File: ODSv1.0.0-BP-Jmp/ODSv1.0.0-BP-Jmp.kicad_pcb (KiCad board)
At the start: 2 copper layers, 150 x 150 mm, 53 parts, among them J1 Conn_01x16, J10 Conn_02x10_Odd_Even, J11 Conn_02x10_Odd_Even, J12 Conn_02x10_Odd_Even, J13 Conn_02x10_Odd_Even, J14 Conn_02x10_Odd_Even, J2 Conn_02x60_Odd_Even, J3 Conn_02x60_Odd_Even, J4 Conn_02x10_Odd_Even, J5 Conn_02x10_Odd_Even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

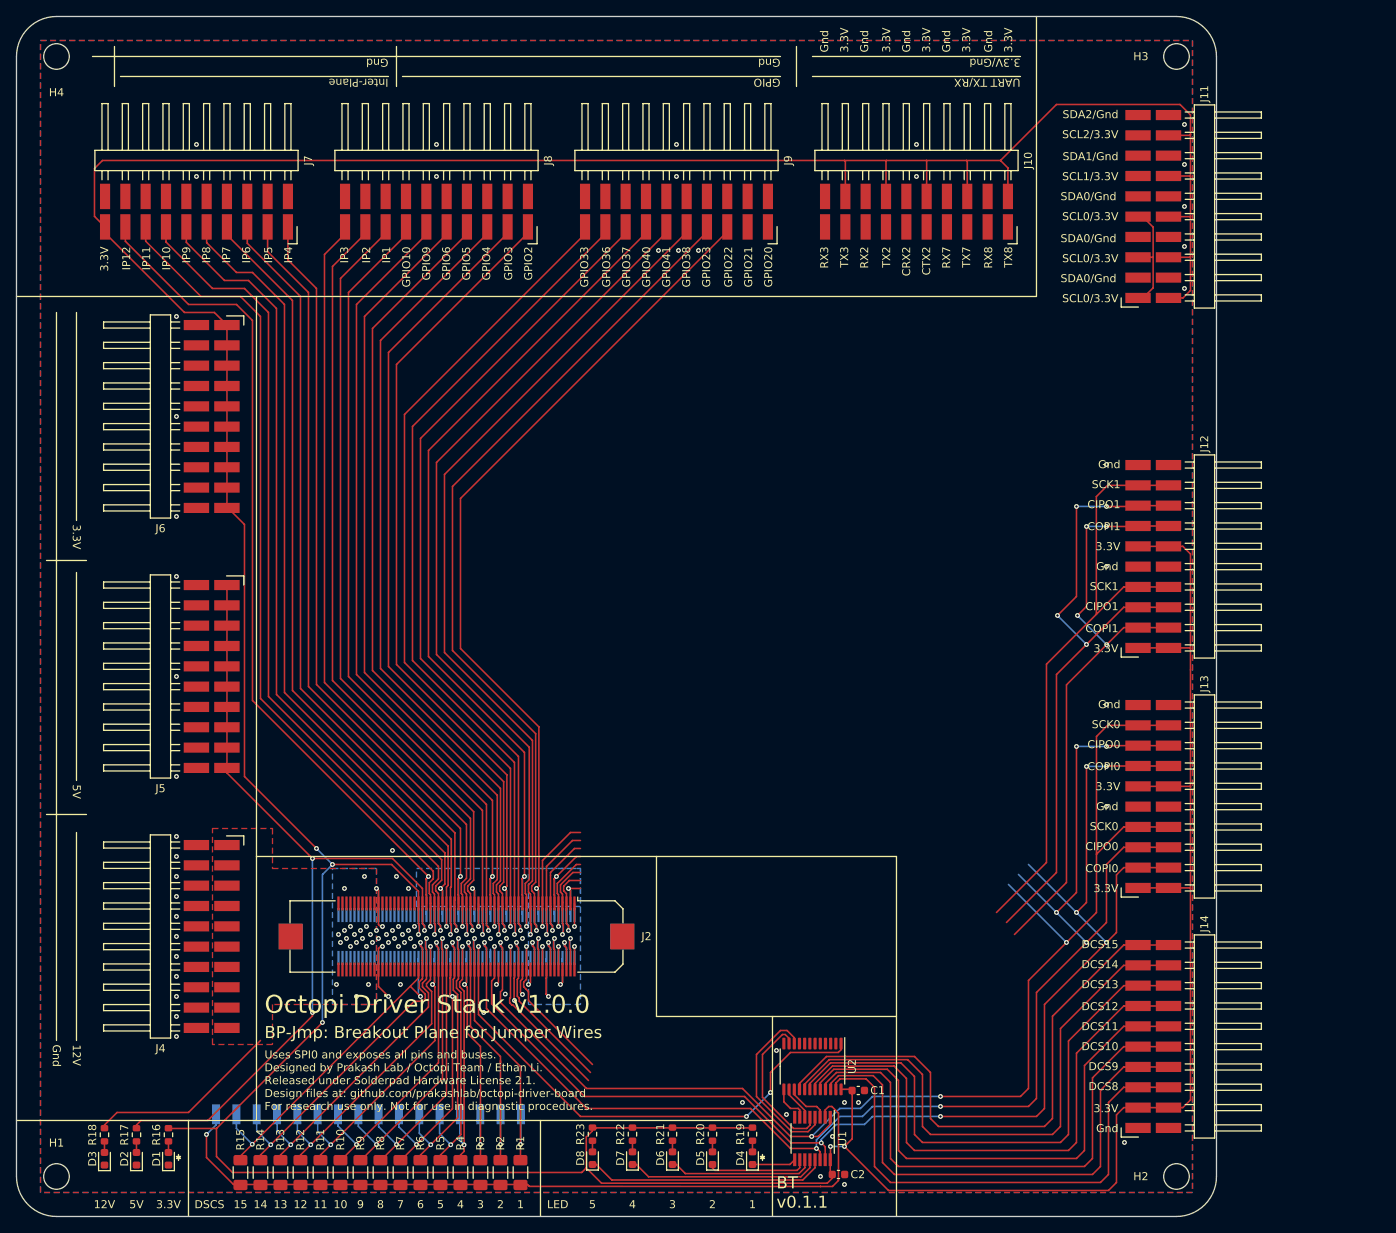
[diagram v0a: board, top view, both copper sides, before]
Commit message: Fix hierarchical pin label directions, finish front right corner
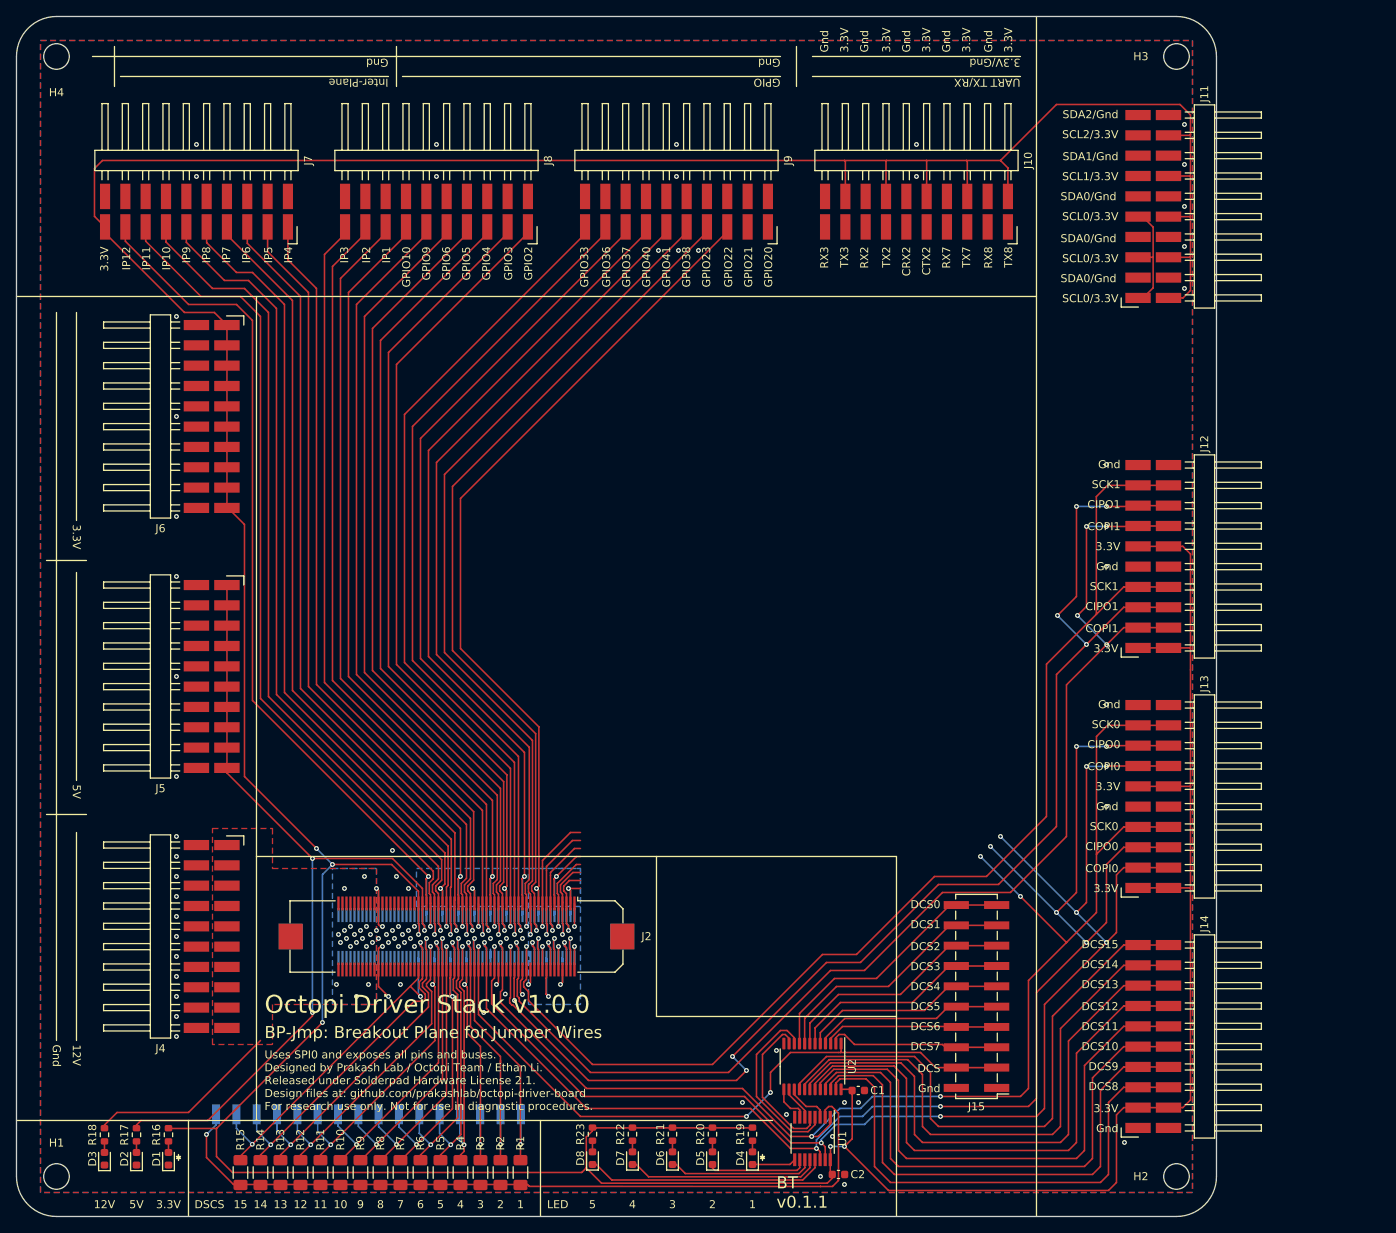
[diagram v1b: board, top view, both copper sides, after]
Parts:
- added J15: Conn_02x10_Odd_Even, Connector_PinHeader_2.54mm:PinHeader_2x10_P2.54mm_Vertical_SMD, F.Cu at (150.0, 182.5)
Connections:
- net /Backbone/SPI DCS Selector/~DCS~ renamed /Backbone/~DCS~
- U2 pad 2: (no net) -> /Backbone/~DCS7~
- U2 pad 3: (no net) -> /Backbone/~DCS6~
- U2 pad 4: (no net) -> /Backbone/~DCS5~
- U2 pad 5: (no net) -> /Backbone/~DCS4~
- U2 pad 6: (no net) -> /Backbone/~DCS3~
- U2 pad 7: (no net) -> /Backbone/~DCS2~
- U2 pad 8: (no net) -> /Backbone/~DCS1~
- U2 pad 9: (no net) -> /Backbone/~DCS0~
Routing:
- net /Backbone/SPI1_CIPO: track 104.7 -> 165.3 mm, vias 5 -> 7
- net /Backbone/SPI1_COPI: track 98.9 -> 155.7 mm
- net /Backbone/SPI1_SCK: track 97.3 -> 152.3 mm
- net /Backbone/~DCS0~: track 0.00 -> 34.0 mm
- net /Backbone/~DCS1~: track 0.00 -> 32.0 mm
- net /Backbone/~DCS2~: track 0.00 -> 29.9 mm
- net /Backbone/~DCS3~: track 0.00 -> 27.9 mm
- net /Backbone/~DCS4~: track 0.00 -> 25.8 mm
- net /Backbone/~DCS5~: track 0.00 -> 23.7 mm
- net /Backbone/~DCS6~: track 0.00 -> 22.0 mm
- net /Backbone/~DCS7~: track 0.00 -> 21.7 mm
- net /Backbone/~DCS~: track 66.2 -> 86.7 mm
- net /Backbone/SPI0_COPI: track 172.0 -> 177.0 mm, vias 7 -> 8
- net /Backbone/SPI0_CIPO: track 178.1 -> 183.0 mm, vias 7 -> 8
- net /Backbone/SPI0_SCK: track 166.8 -> 171.7 mm, vias 4 -> 5
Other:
- board text added: "DCS"
- board text added: "DCS0"
- board text added: "DCS1"
- board text added: "DCS2"
- board text added: "DCS3"
- board text added: "DCS4"
- board text added: "DCS5"
- board text added: "DCS6"
- board text added: "DCS7"

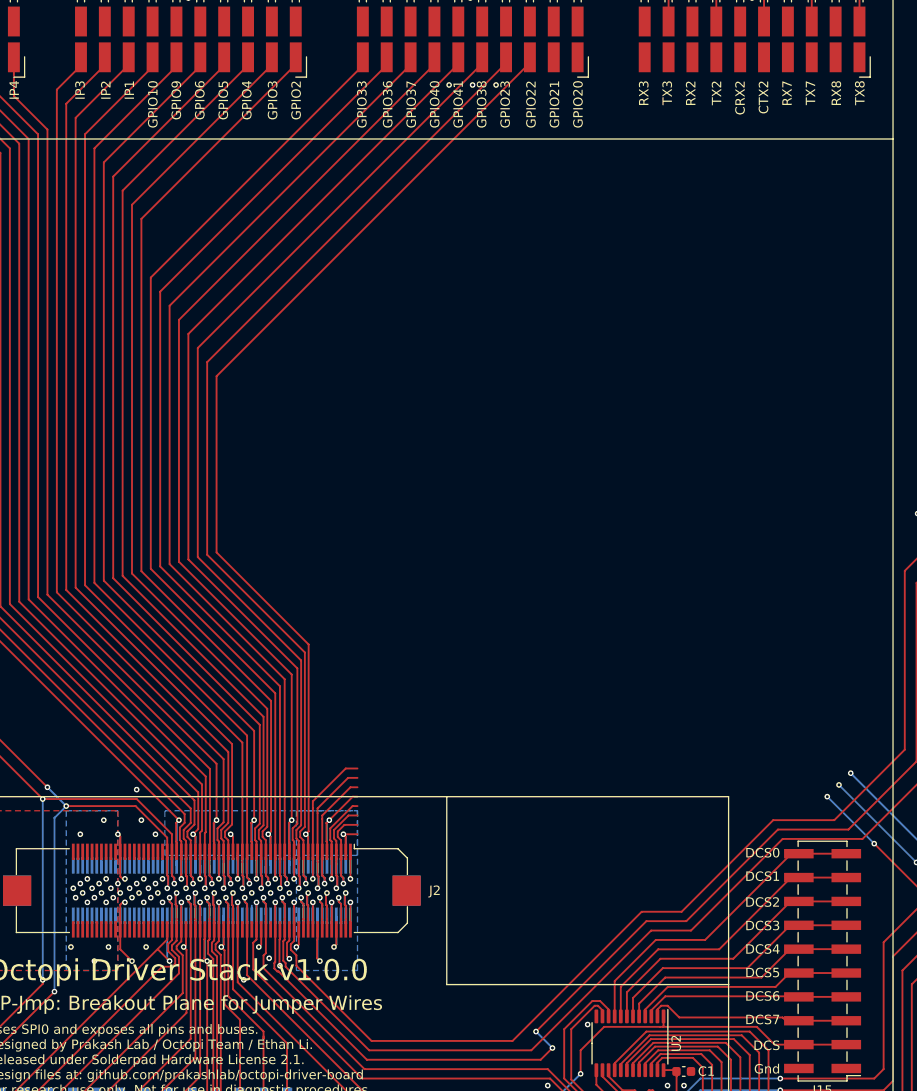
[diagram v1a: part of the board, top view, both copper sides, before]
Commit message: Finish routing GPIO and UART headers
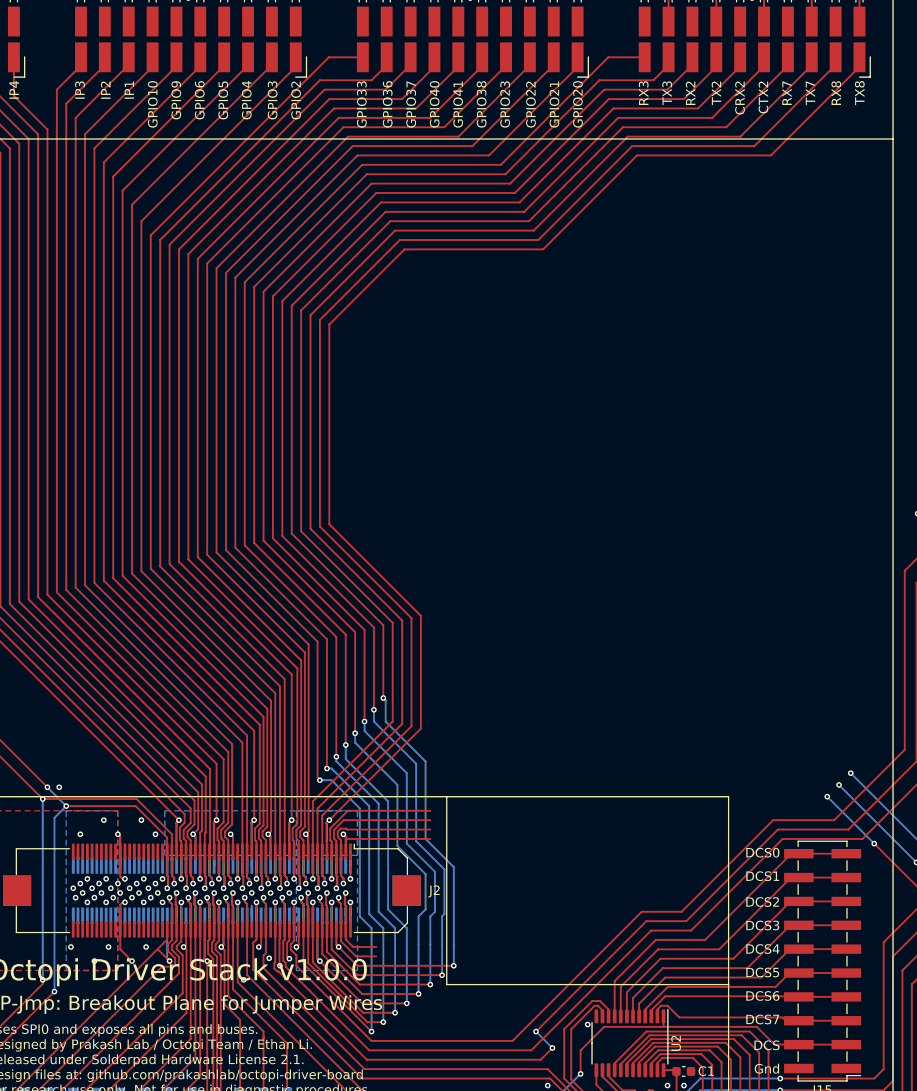
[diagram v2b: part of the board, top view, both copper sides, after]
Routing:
- net /Backbone/CAN2_CRX: track 4.30 -> 158.4 mm, vias 1 -> 3
- net /Backbone/SER2_TX: track 6.47 -> 160.2 mm, vias 1 -> 3
- net /Backbone/SER2_RX: track 5.51 -> 158.8 mm, vias 1 -> 3
- net /Backbone/CAN2_CTX: track 5.41 -> 157.6 mm, vias 1 -> 3
- net /Backbone/SER3_RX: track 4.30 -> 155.6 mm, vias 1 -> 3
- net /Backbone/SER3_TX: track 8.45 -> 157.3 mm, vias 1 -> 3
- net /Backbone/GPIO20: track 6.47 -> 153.5 mm, vias 1 -> 3
- net /Backbone/GPIO21: track 5.51 -> 152.2 mm, vias 1 -> 3
- net /Backbone/SER8_TX: track 12.5 -> 138.1 mm
- net /Backbone/SER8_RX: track 14.4 -> 137.0 mm
- net /Backbone/SER7_TX: track 16.7 -> 136.6 mm
- net /Backbone/SER7_RX: track 15.9 -> 133.0 mm
- net /Backbone/I2C0_SDA: track 10.2 -> 17.8 mm
- net /Backbone/I2C2_SDA: track 10.7 -> 18.3 mm
- net /Backbone/I2C2_SCL: track 12.1 -> 19.7 mm
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
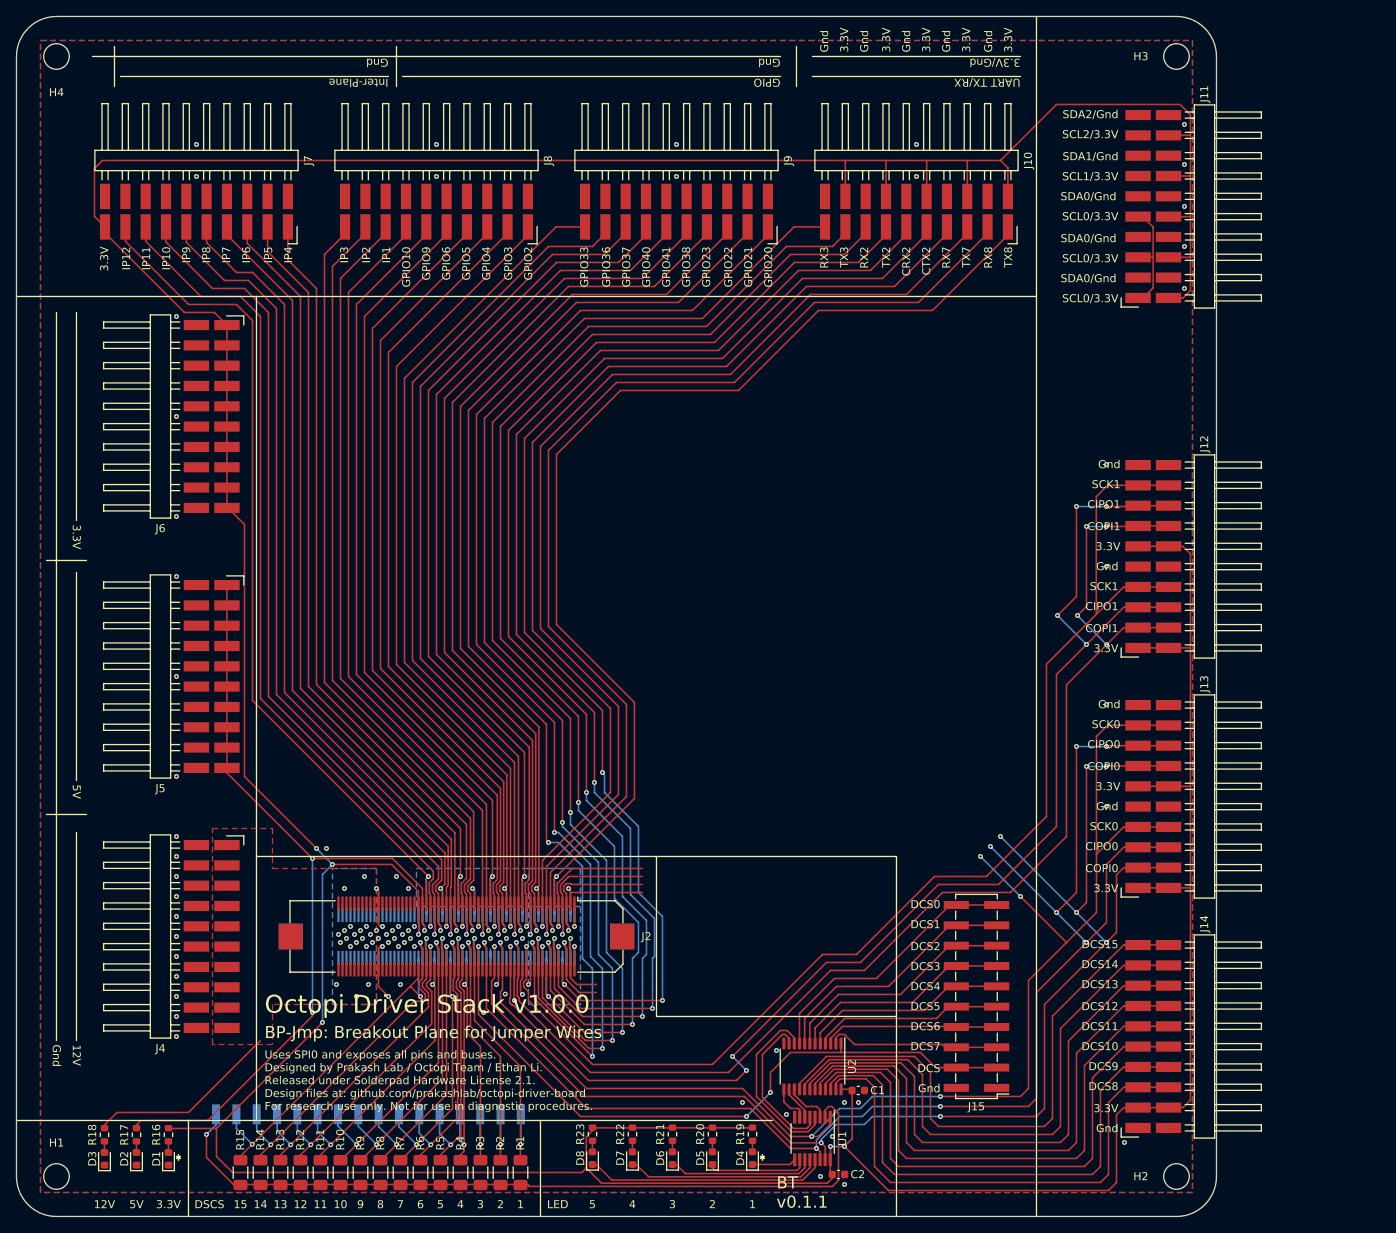
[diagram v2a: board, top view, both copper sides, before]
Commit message: Finish rear right corner
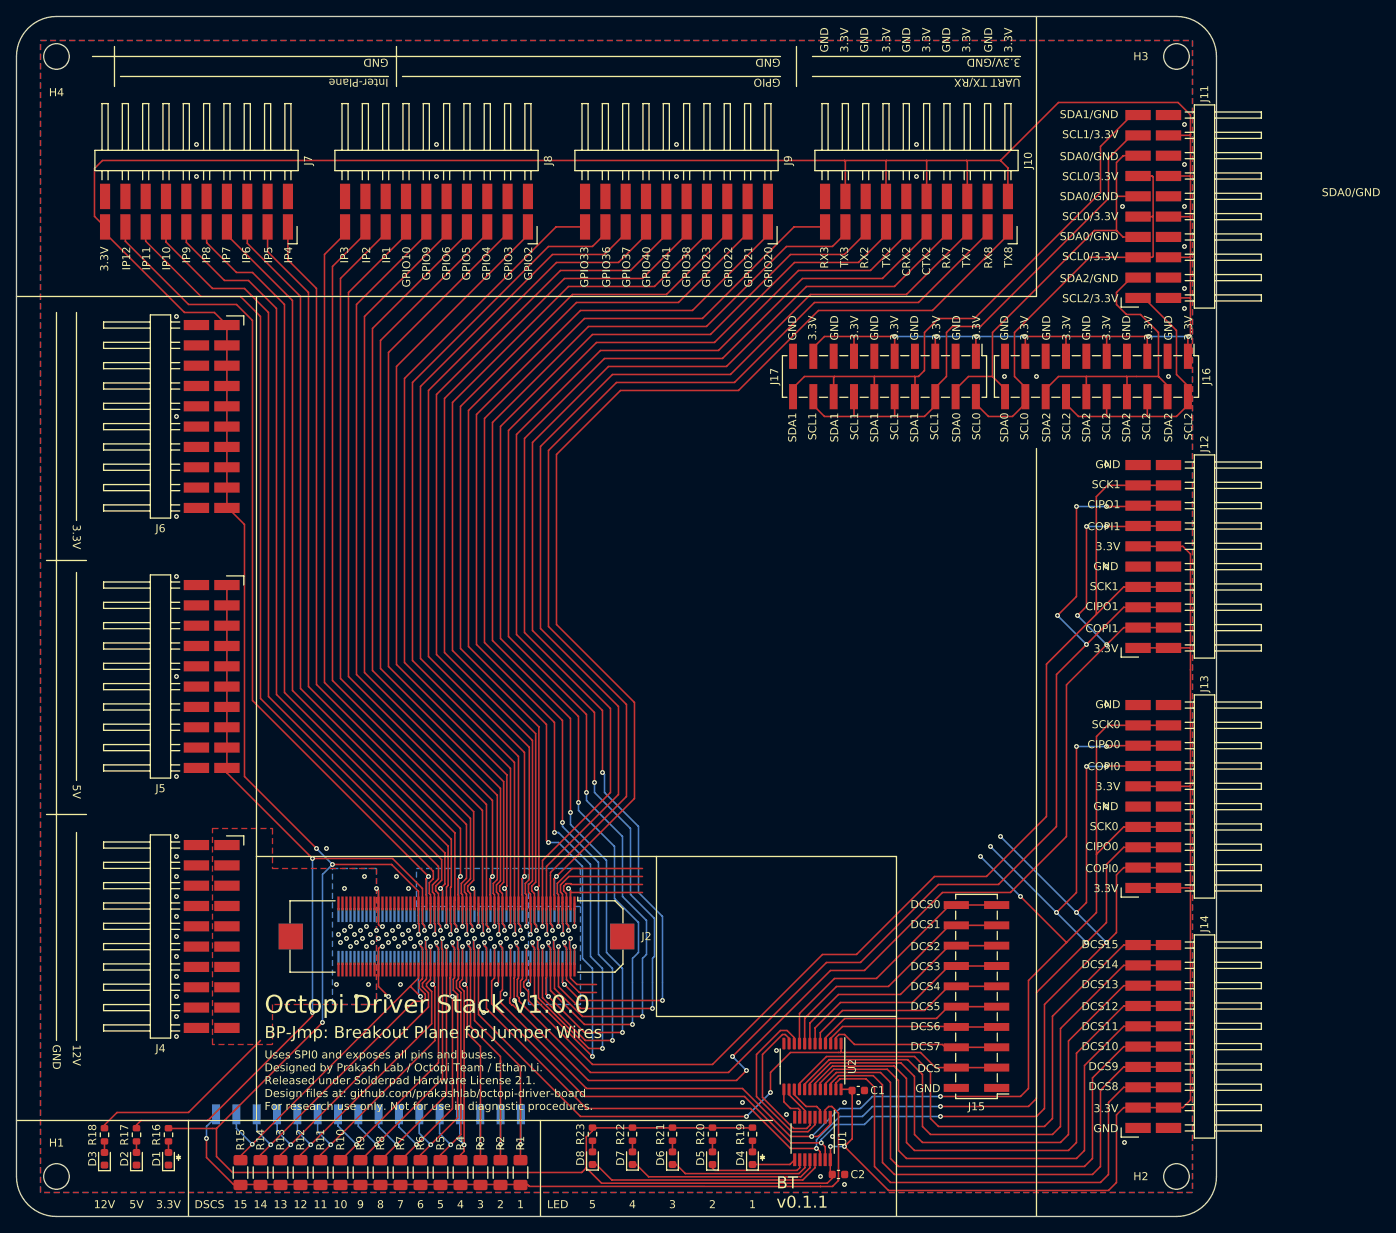
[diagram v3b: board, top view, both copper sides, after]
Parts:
- added J16: Conn_02x10_Odd_Even, Connector_PinHeader_2.54mm:PinHeader_2x10_P2.54mm_Vertical_SMD, F.Cu at (165.0, 105.0)
- added J17: Conn_02x10_Odd_Even, Connector_PinHeader_2.54mm:PinHeader_2x10_P2.54mm_Vertical_SMD, F.Cu at (138.5, 105.0)
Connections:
- J11 pad 14: /Backbone/I2C1_SCL -> /Backbone/I2C0_SCL
- J11 pad 16: /Backbone/I2C1_SDA -> /Backbone/I2C0_SDA
- J11 pad 18: /Backbone/I2C2_SCL -> /Backbone/I2C1_SCL
- J11 pad 2: /Backbone/I2C0_SCL -> /Backbone/I2C2_SCL
- J11 pad 20: /Backbone/I2C2_SDA -> /Backbone/I2C1_SDA
- J11 pad 4: /Backbone/I2C0_SDA -> /Backbone/I2C2_SDA
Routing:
- net +3V3: track 653.3 -> 730.2 mm, vias 9 -> 15
- net /Backbone/I2C1_SDA: track 11.2 -> 84.4 mm
- net /Backbone/I2C1_SCL: track 11.1 -> 80.4 mm
- net /Backbone/I2C0_SDA: track 17.8 -> 70.8 mm
- net /Backbone/I2C2_SDA: track 18.3 -> 60.4 mm
- net /Backbone/I2C2_SCL: track 19.7 -> 59.5 mm
- net /Backbone/I2C0_SCL: track 28.7 -> 67.4 mm
- net GND: vias 74 -> 79
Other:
- board text added: "3.3V/GND"
- board text added: "GND"
- board text added: "SCL0"
- board text added: "SCL1"
- board text added: "SCL2"
- board text added: "SDA0"
- board text added: "SDA0/GND"
- board text added: "SDA1"
- board text added: "SDA1/GND"
- board text added: "SDA2"
- board text added: "SDA2/GND"
- board text removed: "3.3V/Gnd"
- board text removed: "Gnd"
- board text removed: "SDA0/Gnd"
- board text removed: "SDA1/Gnd"
- board text removed: "SDA2/Gnd"
